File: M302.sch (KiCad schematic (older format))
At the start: 13 parts, among them P1 Power, P2 Analog, P3 Digital, P4 Digital, P5 CONN_01X01, P6 CONN_01X01, P7 CONN_01X01, P8 CONN_01X01

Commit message: とりあえず
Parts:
- added C1: 100uF/25V, Capacitor_THT:CP_Radial_D5.0mm_P2.00mm, symbol Device:CP_Small
- added J6: W5500, Connector_PinHeader_2.54mm:PinHeader_2x05_P2.54mm_Vertical, symbol Connector_Generic:Conn_02x05_Counter_Clockwise
- added J7: IM920, Connector_JST:JST_XH_B6B-XH-A_1x06_P2.50mm_Vertical, symbol Connector_Generic:Conn_01x06
- added J8: PWR, Connector_JST:JST_XH_B2B-XH-A_1x02_P2.50mm_Vertical, symbol Connector_Generic:Conn_01x02
- added J9: VSW, Connector_PinHeader_2.54mm:PinHeader_1x03_P2.54mm_Vertical, symbol Connector:Conn_01x03_Male
- added R1: 10k, Resistor_THT:R_Axial_DIN0207_L6.3mm_D2.5mm_P10.16mm_Horizontal, symbol Device:R_US
- added SW1: CPU_RESET, HOLLY:TVDT18-050, symbol Switch:SW_Push
- added SW2: D400_RESET, HOLLY:TVDT18-050, symbol Switch:SW_Push
- added SW3: IM920_RESET, HOLLY:TVDT18-050, symbol Switch:SW_Push
- added U1: SFE-BOB-12009, HOLLY:SFE-BOB-12009, symbol Buffer:SFE-BOB-12009
- J1: renamed from J?; value Conn_01x04 -> I2C-1; footprint (none) -> Connector_JST:JST_XH_B4B-XH-A_1x04_P2.50mm_Vertical
- J2: renamed from J?; value Conn_01x04 -> I2C-2; footprint (none) -> Connector_JST:JST_XH_B4B-XH-A_1x04_P2.50mm_Vertical
- J3: renamed from J?; value Conn_01x04 -> I2C-3; footprint (none) -> Connector_JST:JST_XH_B4B-XH-A_1x04_P2.50mm_Vertical
- J4: renamed from J?; value Conn_01x04 -> I2C-4; footprint (none) -> Connector_JST:JST_XH_B4B-XH-A_1x04_P2.50mm_Vertical
- J5: renamed from J?; value Conn_01x04 -> I2C-D400; footprint (none) -> Connector_JST:JST_XH_B7B-XH-A_1x07_P2.50mm_Vertical; symbol Connector_Generic:Conn_01x04 -> Connector_Generic:Conn_01x07
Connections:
- net +3V3: now also J6.1 (Pin_1), J7.4 (Pin_4), U1.LV
- net +5V: now also J1.2 (Pin_2), J2.2 (Pin_2), J3.2 (Pin_2), J4.2 (Pin_2), J5.1 (Pin_1), J6.10 (Pin_10), J9.1 (Pin_1), R1.1, U1.HV
- net 10(**/SS): now also J6.4 (Pin_4)
- net 11(**/MOSI): now also J6.3 (Pin_3)
- net 12(MISO): now also J6.2 (Pin_2)
- net 13(SCK): now also J6.5 (Pin_5)
- net 4: now also SW3.1, U1.HV1
- net 5(**): now also U1.HV2
- net 6(**): now also U1.HV3
- net 7: now also U1.HV4
- net A3: now also J5.6 (Pin_6), SW2.2
- net A4(SDA): now also J1.3 (Pin_3), J2.3 (Pin_3), J3.3 (Pin_3), J4.3 (Pin_3), J5.4 (Pin_4)
- net A5(SCL): now also J1.4 (Pin_4), J2.4 (Pin_4), J3.4 (Pin_4), J4.4 (Pin_4), J5.7 (Pin_7)
- net GND: now also J1.1 (Pin_1), J2.1 (Pin_1), J3.1 (Pin_1), J4.1 (Pin_1), J5.3 (Pin_3), C1.2, J6.9 (Pin_9), J7.3 (Pin_3), J8.2 (Pin_2), SW1.1, SW2.1, SW3.2, U1.HGND, U1.LGND
- net Reset: now also J6.8 (Pin_8), R1.2, SW1.2
- net Vin: now also J9.3 (Pin_3)
- new net: J7.1 (Pin_1), U1.LV1
- new net: J7.2 (Pin_2), U1.LV2
- new net: J7.5 (Pin_5), U1.LV3
- new net: J7.6 (Pin_6), U1.LV4
- new net: C1.1, J8.1 (Pin_1), J9.2 (Pin_2)
- no-connect marks 5 -> 16
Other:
- note added: "IM920 BUSY"
- note added: "IM920 RESET"
- note added: "RX(IM920 TX)"
- note added: "TX(IM920 RX)"
- moved on the sheet: J1, J2, J3, J4, P1, P2, P3, P4, P5, P6, P7, P8

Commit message: VSWは不要なので外す
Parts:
- J6: symbol Connector_Generic:Conn_02x05_Counter_Clockwise -> Connector_Generic:Conn_02x05_Odd_Even
- SW1: value CPU_RESET -> CPU
- SW2: value D400_RESET -> D400
- SW3: value IM920_RESET -> IM920
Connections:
- net +5V: now also J6.2 (Pin_2); no longer J6.10 (Pin_10)
- net 10(**/SS): now also J6.7 (Pin_7); no longer J6.4 (Pin_4)
- net 11(**/MOSI): now also J6.5 (Pin_5); no longer J6.3 (Pin_3)
- net 12(MISO): now also J6.3 (Pin_3); no longer J6.2 (Pin_2)
- net 13(SCK): now also J6.9 (Pin_9); no longer J6.5 (Pin_5)
- net 4: now also U1.HV4; no longer U1.HV1
- net 5(**): now also U1.HV3; no longer U1.HV2
- net 6(**): now also U1.HV2; no longer U1.HV3
- net 7: now also U1.HV1; no longer U1.HV4
- net GND: now also J6.4 (Pin_4); no longer J6.9 (Pin_9)
- net Reset: now also J6.6 (Pin_6); no longer J6.8 (Pin_8)
- net at U1.LV1: now also J7.6 (Pin_6); no longer J7.1 (Pin_1)
- net at U1.LV2: now also J7.5 (Pin_5); no longer J7.2 (Pin_2)
- net at U1.LV3: now also J7.2 (Pin_2); no longer J7.5 (Pin_5)
- net at U1.LV4: now also J7.1 (Pin_1); no longer J7.6 (Pin_6)
- no-connect marks 16 -> 14
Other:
- note added: "RESET"
- moved on the sheet: SW3
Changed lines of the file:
@@
 	7150 3400 7500 3400
-Wire Wire Line
-	7150 3300 7500 3300
-Wire Wire Line
-	7150 3200 7500 3200
 Wire Wire Line
 	7150 5000 7500 5000
@@
 Connection ~ 4950 5000
 Wire Wire Line
-	4950 5000 6350 5000
+	4950 5000 5300 5000
 Wire Wire Line
 	4650 4500 4650 4900
 Connection ~ 4650 4900
 Wire Wire Line
-	4650 4900 6350 4900
+	4650 4900 5400 4900
 Wire Wire Line
 	4350 4500 4350 4600
@@
 P 4350 5400
 F 0 "SW2" H 4350 5685 50  0000 C CNN
-F 1 "D400_RESET" H 4350 5594 50  0000 C CNN
+F 1 "D400" H 4350 5594 50  0000 C CNN
 F 2 "HOLLY:TVDT18-050" H 4350 5600 50  0001 C CNN
 F 3 "~" H 4350 5600 50  0001 C CNN
@@
 P 4450 3800
 F 0 "SW1" H 4450 4085 50  0000 C CNN
-F 1 "CPU_RESET" H 4450 3994 50  0000 C CNN
+F 1 "CPU" H 4450 3994 50  0000 C CNN
 F 2 "HOLLY:TVDT18-050" H 4450 4000 50  0001 C CNN
 F 3 "~" H 4450 4000 50  0001 C CNN
@@
 	4100 3800 4100 3950
 $Comp
-L Connector_Generic:Conn_02x05_Counter_Clockwise J6
+L Connector_Generic:Conn_02x05_Odd_Even J6
 U 1 1 5F839511
 P 9300 2900
@@
 	7150 3800 8650 3800
 Wire Wire Line
-	8700 3900 8700 3000
-Wire Wire Line
 	8700 3000 9100 3000
 Wire Wire Line
@@
 Wire Wire Line
 	7150 3600 8750 3600
-NoConn ~ 7500 3200
-NoConn ~ 7500 3300
 NoConn ~ 7500 3400
 NoConn ~ 6300 3450
@@
 L Buffer:SFE-BOB-12009 U1
 U 1 1 5F77B0BE
-P 9050 4250
-F 0 "U1" H 9050 4275 50  0000 C CNN
-F 1 "SFE-BOB-12009" H 9050 4184 50  0000 C CNN
-F 2 "HOLLY:SFE-BOB-12009" H 9050 4250 50  0001 C CNN
-F 3 "" H 9050 4250 50  0001 C CNN
-	1    9050 4250
-	-1   0    0    -1
+P 9050 5150
+F 0 "U1" H 9050 5175 50  0000 C CNN
+F 1 "SFE-BOB-12009" H 9050 5084 50  0000 C CNN
+F 2 "HOLLY:SFE-BOB-12009" H 9050 5150 50  0001 C CNN
+F 3 "" H 9050 5150 50  0001 C CNN
+	1    9050 5150
+	-1   0    0    1
 $EndComp
 Wire Wire Line
@@
 $EndComp
 Wire Wire Line
-	9400 4650 9650 4650
-Wire Wire Line
-	8700 4650 8400 4650
-Wire Wire Line
-	8400 4650 8400 5250
-Wire Wire Line
-	8400 5250 9650 5250
-Connection ~ 9650 5250
-Wire Wire Line
-	9650 5250 9650 5500
-Connection ~ 9650 4750
-Wire Wire Line
-	9650 4750 9650 5250
-Wire Wire Line
 	9650 4750 9950 4750
-Wire Wire Line
-	9650 4650 9650 4750
-$Comp
-L power:+3.3V #PWR0110
-U 1 1 5F7EDC68
-P 9450 4200
-F 0 "#PWR0110" H 9450 4050 50  0001 C CNN
-F 1 "+3.3V" V 9450 4450 50  0000 C CNN
-F 2 "" H 9450 4200 50  0000 C CNN
-F 3 "" H 9450 4200 50  0000 C CNN
-	1    9450 4200
-	1    0    0    -1
-$EndComp
 $Comp
 L power:+3.3V #PWR0111
 U 1 1 5F7EE56D
-P 9750 4200
-F 0 "#PWR0111" H 9750 4050 50  0001 C CNN
-F 1 "+3.3V" V 9750 4450 50  0000 C CNN
-F 2 "" H 9750 4200 50  0000 C CNN
-F 3 "" H 9750 4200 50  0000 C CNN
-	1    9750 4200
-	1    0    0    -1
-$EndComp
-Wire Wire Line
-	9750 4200 9750 4650
-Wire Wire Line
-	9750 4650 9950 4650
+P 9650 4200
+F 0 "#PWR0111" H 9650 4050 50  0001 C CNN
+F 1 "+3.3V" V 9650 4450 50  0000 C CNN
+F 2 "" H 9650 4200 50  0000 C CNN
+F 3 "" H 9650 4200 50  0000 C CNN
+	1    9650 4200
+	1    0    0    -1
+$EndComp
+Wire Wire Line
+	9650 4200 9650 4650
+Wire Wire Line
+	9650 4650 9950 4650
 Wire Wire Line
 	9400 4850 9950 4850
@@
 L power:+5V #PWR0112
 U 1 1 5F803107
-P 8450 4150
-F 0 "#PWR0112" H 8450 4000 50  0001 C CNN
-F 1 "+5V" V 8450 4350 50  0000 C CNN
-F 2 "" H 8450 4150 50  0000 C CNN
-F 3 "" H 8450 4150 50  0000 C CNN
-	1    8450 4150
-	1    0    0    -1
-$EndComp
-Wire Wire Line
-	8700 4750 8450 4750
-Wire Wire Line
-	8450 4750 8450 4150
+P 8500 4200
+F 0 "#PWR0112" H 8500 4050 50  0001 C CNN
+F 1 "+5V" V 8500 4400 50  0000 C CNN
+F 2 "" H 8500 4200 50  0000 C CNN
+F 3 "" H 8500 4200 50  0000 C CNN
+	1    8500 4200
+	1    0    0    -1
+$EndComp
 Wire Wire Line
 	8200 4300 8200 4450
@@
 Wire Wire Line
 	8050 4600 8050 4950
-Wire Wire Line
-	8050 4950 8550 4950
 Wire Wire Line
 	7150 4600 8050 4600
@@
 Text Notes 8200 4500 0    39   ~ 0
 TX(IM920 RX)
-Wire Wire Line
-	9450 4200 9450 4750
-Wire Wire Line
-	9450 4750 9400 4750
 $Comp
 L Switch:SW_Push SW3
 U 1 1 5F84E5BD
-P 8550 5600
-F 0 "SW3" H 8550 5885 50  0000 C CNN
-F 1 "IM920_RESET" H 8550 5794 50  0000 C CNN
-F 2 "HOLLY:TVDT18-050" H 8550 5800 50  0001 C CNN
-F 3 "~" H 8550 5800 50  0001 C CNN
-	1    8550 5600
+P 8050 5600
+F 0 "SW3" H 8050 5885 50  0000 C CNN
+F 1 "IM920" H 8050 5794 50  0000 C CNN
+F 2 "HOLLY:TVDT18-050" H 8050 5800 50  0001 C CNN
+F 3 "~" H 8050 5800 50  0001 C CNN
+	1    8050 5600
 	0    1    1    0
 $EndComp
@@
 L power:GND #PWR0113
 U 1 1 5F84F736
-P 8550 6000
-F 0 "#PWR0113" H 8550 5750 50  0001 C CNN
-F 1 "GND" H 8550 5850 50  0000 C CNN
-F 2 "" H 8550 6000 50  0000 C CNN
-F 3 "" H 8550 6000 50  0000 C CNN
-	1    8550 6000
-	1    0    0    -1
-$EndComp
-Wire Wire Line
-	8550 6000 8550 5800
-Wire Wire Line
-	8550 5400 8550 4950
-Connection ~ 8550 4950
-Wire Wire Line
-	8550 4950 8700 4950
+P 8050 6050
+F 0 "#PWR0113" H 8050 5800 50  0001 C CNN
+F 1 "GND" H 8050 5900 50  0000 C CNN
+F 2 "" H 8050 6050 50  0000 C CNN
+F 3 "" H 8050 6050 50  0000 C CNN
+	1    8050 6050
+	1    0    0    -1
+$EndComp
+Wire Wire Line
+	8050 6050 8050 5800
+Wire Wire Line
+	8050 5400 8050 4950
+Connection ~ 8050 4950
+Wire Wire Line
+	8050 4950 8700 4950
+Wire Wire Line
+	9650 4750 9650 5300
+Wire Wire Line
+	9400 4750 9650 4750
+Connection ~ 9650 4750
+Wire Wire Line
+	9650 4650 9400 4650
+Connection ~ 9650 4650
+Wire Wire Line
+	8700 3000 8700 3900
+Wire Wire Line
+	8500 4200 8500 4650
+Wire Wire Line
+	8500 4650 8700 4650
+Wire Wire Line
+	8700 4750 8500 4750
+Wire Wire Line
+	8500 4750 8500 5300
+Wire Wire Line
+	8500 5300 9650 5300
+Connection ~ 9650 5300
+Wire Wire Line
+	9650 5300 9650 5500
+Text Notes 4350 3900 0    50   ~ 0
+RESET
+Text Notes 4250 5500 0    50   ~ 0
+RESET
+Text Notes 8000 5700 1    50   ~ 0
+RESET
+Wire Wire Line
+	5400 4900 5400 2250
+Wire Wire Line
+	5400 2250 8350 2250
+Wire Wire Line
+	8350 2250 8350 3300
+Wire Wire Line
+	7150 3300 8350 3300
+Connection ~ 5400 4900
+Wire Wire Line
+	5400 4900 6350 4900
+Wire Wire Line
+	5300 5000 5300 2150
+Wire Wire Line
+	5300 2150 8250 2150
+Wire Wire Line
+	8250 2150 8250 3200
+Wire Wire Line
+	7150 3200 8250 3200
+Connection ~ 5300 5000
+Wire Wire Line
+	5300 5000 6350 5000
 $EndSCHEMATC

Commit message: 現在基板確認中
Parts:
- removed J9: VSW, Connector_PinHeader_2.54mm:PinHeader_1x03_P2.54mm_Vertical, symbol Connector:Conn_01x03_Male
- J1: value I2C-1 -> I2C-SHT3x
- J2: value I2C-2 -> I2C-ThmCp
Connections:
- net +5V: now also C1.1, J8.1 (Pin_1)
- net Vin: no longer P1.8 (Pin_8)
- no-connect marks 14 -> 21
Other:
- moved on the sheet: C1, J8
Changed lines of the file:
@@
 Sheet 1 1
 Title "M302 Measurement Equipment Type Light"
-Date "2020-10-03"
+Date "2020-10-04"
 Rev "1.00"
 Comp "HOLLY&Co.,Ltd."
@@
 Wire Wire Line
 	6350 4200 6250 4200
-Connection ~ 6250 4200
 Wire Wire Line
 	6000 4000 6000 3350
@@
 Wire Wire Line
 	6250 4100 6250 4200
-Wire Wire Line
-	6250 4200 6250 5150
 Wire Notes Line
 	5450 2500 5450 5450
@@
 U 1 1 5F8861FD
 P 2400 4300
-F 0 "J2" V 2500 4450 50  0000 R CNN
-F 1 "I2C-2" V 2500 4250 50  0000 R CNN
+F 0 "J2" V 2600 4450 50  0000 R CNN
+F 1 "I2C-ThmCp" V 2500 4450 50  0000 R CNN
 F 2 "Connector_JST:JST_XH_B4B-XH-A_1x04_P2.50mm_Vertical" H 2400 4300 50  0001 C CNN
 F 3 "~" H 2400 4300 50  0001 C CNN
@@
 U 1 1 5F886759
 P 1750 4300
-F 0 "J1" V 1850 4450 50  0000 R CNN
-F 1 "I2C-1" V 1850 4250 50  0000 R CNN
+F 0 "J1" V 1950 4450 50  0000 R CNN
+F 1 "I2C-SHT3x" V 1850 4450 50  0000 R CNN
 F 2 "Connector_JST:JST_XH_B4B-XH-A_1x04_P2.50mm_Vertical" H 1750 4300 50  0001 C CNN
 F 3 "~" H 1750 4300 50  0001 C CNN
@@
 L Connector_Generic:Conn_01x02 J8
 U 1 1 5F897A65
-P 1950 2450
-F 0 "J8" H 1868 2667 50  0000 C CNN
-F 1 "PWR" H 1868 2576 50  0000 C CNN
-F 2 "Connector_JST:JST_XH_B2B-XH-A_1x02_P2.50mm_Vertical" H 1950 2450 50  0001 C CNN
-F 3 "~" H 1950 2450 50  0001 C CNN
-	1    1950 2450
+P 1700 1700
+F 0 "J8" H 1618 1917 50  0000 C CNN
+F 1 "PWR" H 1618 1826 50  0000 C CNN
+F 2 "Connector_JST:JST_XH_B2B-XH-A_1x02_P2.50mm_Vertical" H 1700 1700 50  0001 C CNN
+F 3 "~" H 1700 1700 50  0001 C CNN
+	1    1700 1700
 	-1   0    0    -1
 $EndComp
-$Comp
-L Connector:Conn_01x03_Male J9
-U 1 1 5F8A1D1C
-P 3800 2100
-F 0 "J9" V 3862 2244 50  0000 L CNN
-F 1 "VSW" V 3953 2244 50  0000 L CNN
-F 2 "Connector_PinHeader_2.54mm:PinHeader_1x03_P2.54mm_Vertical" H 3800 2100 50  0001 C CNN
-F 3 "~" H 3800 2100 50  0001 C CNN
-	1    3800 2100
-	0    1    1    0
-$EndComp
-Wire Wire Line
-	2150 2450 2850 2450
-Wire Wire Line
-	3800 2450 3800 2300
-Wire Wire Line
-	3700 2300 3700 2950
-Wire Wire Line
-	3700 2950 5900 2950
-Wire Wire Line
-	5900 2950 5900 4300
+Wire Wire Line
+	1900 1700 2600 1700
+Wire Wire Line
+	3550 1700 3550 1550
 $Comp
 L power:GND #PWR0107
 U 1 1 5F8AB9C5
-P 2150 2850
-F 0 "#PWR0107" H 2150 2600 50  0001 C CNN
-F 1 "GND" H 2155 2677 50  0000 C CNN
-F 2 "" H 2150 2850 50  0001 C CNN
-F 3 "" H 2150 2850 50  0001 C CNN
-	1    2150 2850
-	1    0    0    -1
-$EndComp
-Wire Wire Line
-	2150 2550 2150 2750
+P 1900 2100
+F 0 "#PWR0107" H 1900 1850 50  0001 C CNN
+F 1 "GND" H 1905 1927 50  0000 C CNN
+F 2 "" H 1900 2100 50  0001 C CNN
+F 3 "" H 1900 2100 50  0001 C CNN
+	1    1900 2100
+	1    0    0    -1
+$EndComp
+Wire Wire Line
+	1900 1800 1900 2000
 $Comp
 L power:+5V #PWR0105
 U 1 1 5F8B4AD0
-P 4400 2300
-F 0 "#PWR0105" H 4400 2150 50  0001 C CNN
-F 1 "+5V" V 4400 2500 50  0000 C CNN
-F 2 "" H 4400 2300 50  0000 C CNN
-F 3 "" H 4400 2300 50  0000 C CNN
-	1    4400 2300
-	1    0    0    -1
-$EndComp
-Wire Wire Line
-	3900 2300 3900 2450
-Wire Wire Line
-	3900 2450 4400 2450
-Wire Wire Line
-	4400 2450 4400 2300
+P 3550 1550
+F 0 "#PWR0105" H 3550 1400 50  0001 C CNN
+F 1 "+5V" V 3550 1750 50  0000 C CNN
+F 2 "" H 3550 1550 50  0000 C CNN
+F 3 "" H 3550 1550 50  0000 C CNN
+	1    3550 1550
+	1    0    0    -1
+$EndComp
 $Comp
 L Device:CP_Small C1
 U 1 1 5F8BA3B3
-P 2850 2600
-F 0 "C1" H 2938 2646 50  0000 L CNN
-F 1 "100uF/25V" H 2938 2555 50  0000 L CNN
-F 2 "Capacitor_THT:CP_Radial_D5.0mm_P2.00mm" H 2850 2600 50  0001 C CNN
-F 3 "https://akizukidenshi.com/download/ds/rubycon/PK_series.pdf" H 2850 2600 50  0001 C CNN
-	1    2850 2600
-	1    0    0    -1
-$EndComp
-Wire Wire Line
-	2850 2500 2850 2450
-Connection ~ 2850 2450
-Wire Wire Line
-	2850 2450 3800 2450
-Wire Wire Line
-	2850 2700 2850 2750
-Wire Wire Line
-	2850 2750 2150 2750
-Connection ~ 2150 2750
-Wire Wire Line
-	2150 2750 2150 2850
+P 2600 1850
+F 0 "C1" H 2688 1896 50  0000 L CNN
+F 1 "100uF/25V" H 2688 1805 50  0000 L CNN
+F 2 "Capacitor_THT:CP_Radial_D5.0mm_P2.00mm" H 2600 1850 50  0001 C CNN
+F 3 "https://akizukidenshi.com/download/ds/rubycon/PK_series.pdf" H 2600 1850 50  0001 C CNN
+	1    2600 1850
+	1    0    0    -1
+$EndComp
+Wire Wire Line
+	2600 1750 2600 1700
+Connection ~ 2600 1700
+Wire Wire Line
+	2600 1700 3550 1700
+Wire Wire Line
+	2600 1950 2600 2000
+Wire Wire Line
+	2600 2000 1900 2000
+Connection ~ 1900 2000
+Wire Wire Line
+	1900 2000 1900 2100
 $Comp
 L Buffer:SFE-BOB-12009 U1
@@
 Wire Wire Line
 	5300 5000 6350 5000
+Wire Wire Line
+	5900 3500 5900 4300
+NoConn ~ 5900 3500
+NoConn ~ 7500 4100
+NoConn ~ 7500 4000
+NoConn ~ 7500 4700
+NoConn ~ 7500 4800
+NoConn ~ 7500 4900
+NoConn ~ 7500 5000
+Connection ~ 6250 4200
+Wire Wire Line
+	6250 4200 6250 5150
 $EndSCHEMATC

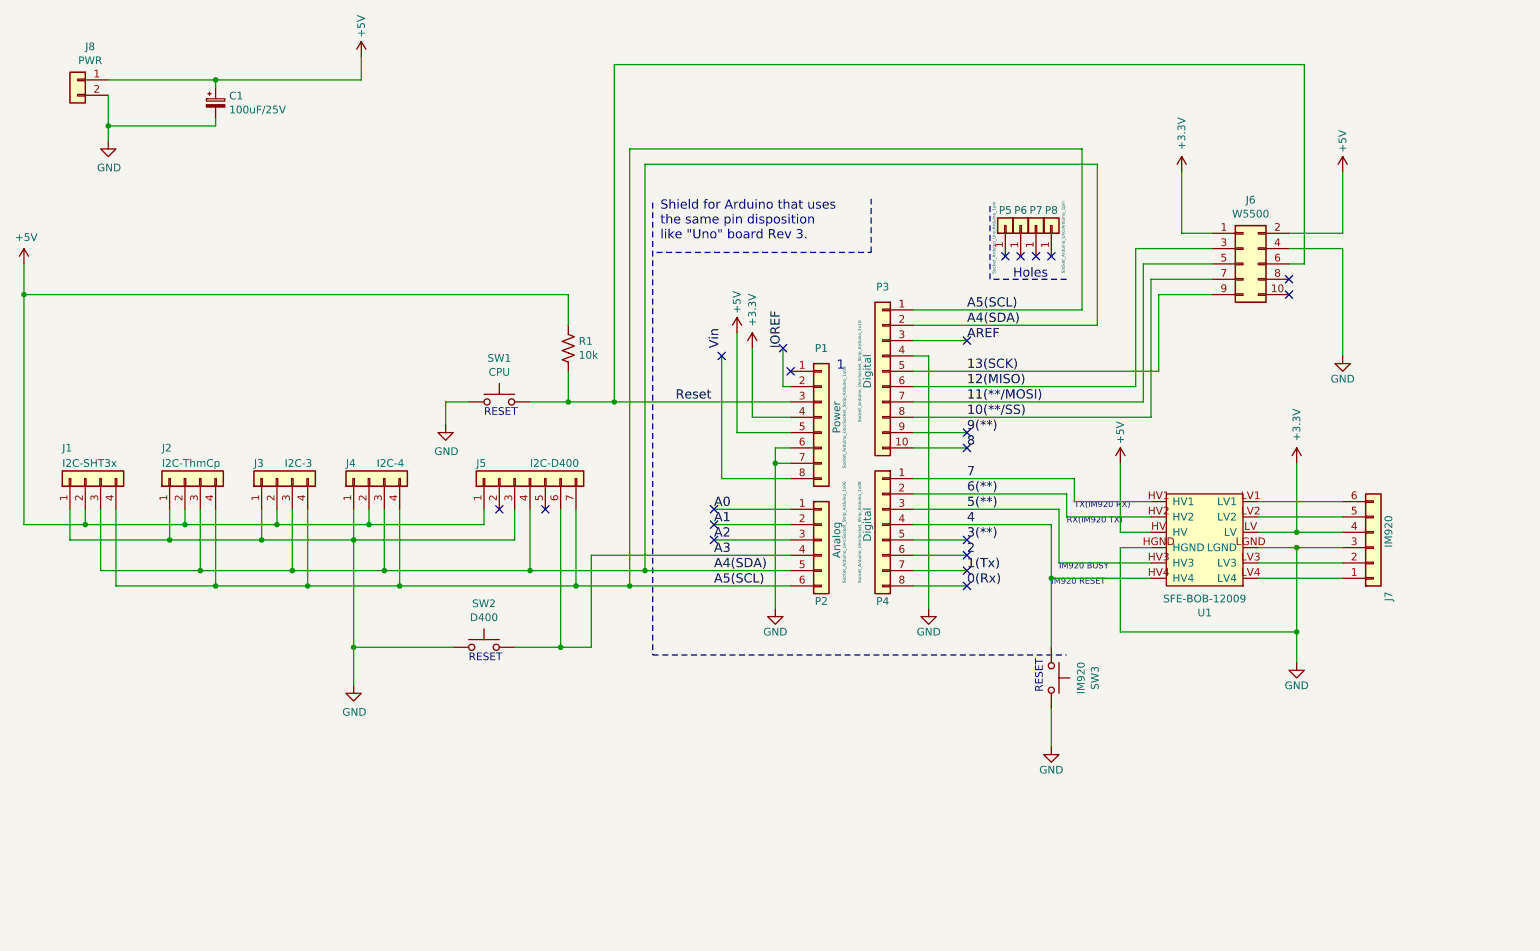
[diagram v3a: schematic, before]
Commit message: sch: 1.10 PullUp抵抗とアナログインプットを増やす
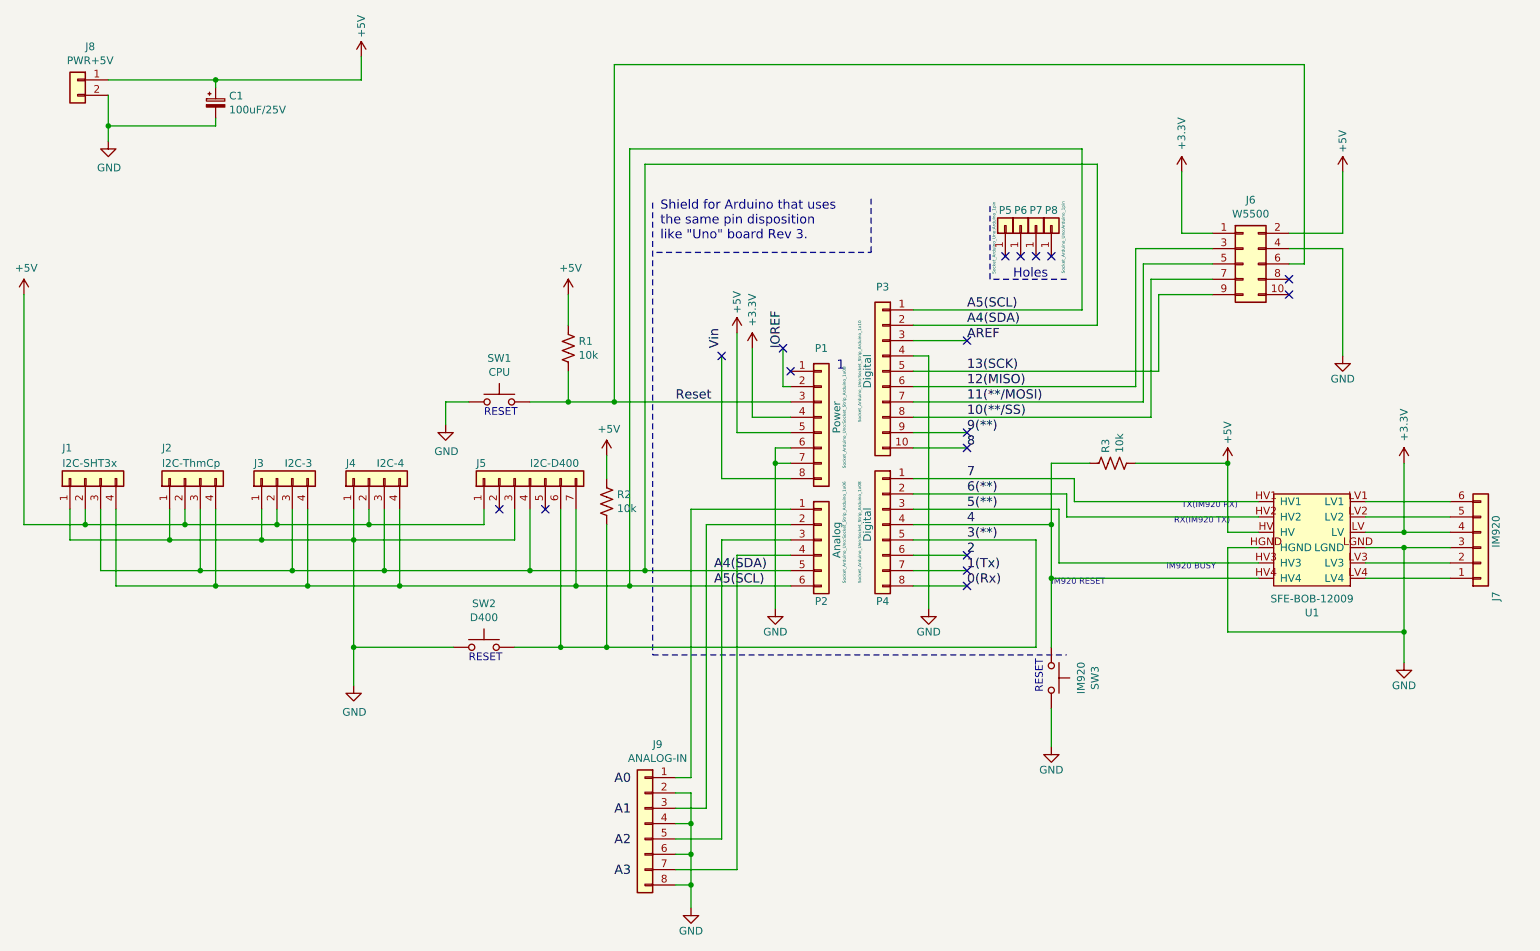
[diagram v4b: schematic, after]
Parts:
- added J9: ANALOG-IN, Connector_JST:JST_XH_B8B-XH-A_1x08_P2.50mm_Vertical, symbol Connector_Generic:Conn_01x08
- added R2, R3: 10k, Resistor_THT:R_Axial_DIN0207_L6.3mm_D2.5mm_P10.16mm_Horizontal, symbol Device:R_US
- J8: value PWR -> PWR+5V
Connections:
- net +5V: now also R2.1, R3.2
- net 3(**): now also J5.6 (Pin_6), SW2.2, R2.2
- net 4: now also R3.1
- net A0: no longer P2.1 (Pin_1)
- net A1: no longer P2.2 (Pin_2)
- net A2: no longer P2.3 (Pin_3)
- net A3: no longer J5.6 (Pin_6), P2.4 (Pin_4), SW2.2
- net GND: now also J9.2 (Pin_2), J9.4 (Pin_4), J9.6 (Pin_6), J9.8 (Pin_8)
- new net: J9.1 (Pin_1), P2.1 (Pin_1)
- new net: J9.3 (Pin_3), P2.2 (Pin_2)
- new net: J9.5 (Pin_5), P2.3 (Pin_3)
- new net: J9.7 (Pin_7), P2.4 (Pin_4)
- no-connect marks 21 -> 17
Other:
- moved on the sheet: J7, U1
